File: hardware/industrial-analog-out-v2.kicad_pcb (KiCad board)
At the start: 2 copper layers, 40 x 40 mm, 54 parts, among them P1 CON-SENSOR2, P2 CONN_8, P3 DEBUG, P4 BOOT, U1 LMR62014X, U2 XMC1XXX24, U3 DACX760, U4 DRILL, U5 DRILL, U6 DRILL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

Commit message: fix fiducials
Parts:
- D5, D6: value LED -> blue
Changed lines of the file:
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@@
-(kicad_pcb (version 4) (host pcbnew 4.0.7-e2-6376~58~ubuntu17.04.1)
+(kicad_pcb (version 4) (host pcbnew 4.0.7-e2-6376~61~ubuntu18.04.1)
   (general
     (links 115)
@@
     (mod_text_size 1.5 1.5)
     (mod_text_width 0.15)
-    (pad_size 0.45 1.75)
+    (pad_size 1.00076 1.00076)
     (pad_drill 0)
     (pad_to_mask_clearance 0)
@@
     )
     (fp_circle (center 0 0) (end 1.15062 0) (layer Dwgs.User) (width 0.01016))
-    (pad 1 smd circle (at 0 0) (size 1.00076 1.00076) (layers F.Cu F.Mask)
+    (pad 1 smd circle (at 0 0) (size 1.00076 1.00076) (layers F.Cu F.Paste F.Mask)
       (clearance 0.65024))
   )
@@
     )
     (fp_circle (center 0 0) (end 1.15062 0) (layer Dwgs.User) (width 0.01016))
-    (pad 1 smd circle (at 0 0) (size 1.00076 1.00076) (layers F.Cu F.Mask)
+    (pad 1 smd circle (at 0 0) (size 1.00076 1.00076) (layers F.Cu F.Paste F.Mask)
       (clearance 0.65024))
   )
@@
     )
     (fp_circle (center 0 0) (end 1.15062 0) (layer Dwgs.User) (width 0.01016))
-    (pad 1 smd circle (at 0 0) (size 1.00076 1.00076) (layers F.Cu F.Mask)
+    (pad 1 smd circle (at 0 0) (size 1.00076 1.00076) (layers F.Cu F.Paste F.Mask)
       (clearance 0.65024))
   )
@@
       (effects (font (size 0.2 0.2) (thickness 0.05)))
     )
-    (fp_text value LED (at 0.75 0.45 270) (layer F.Fab)
+    (fp_text value blue (at 0.75 0.45 270) (layer F.Fab)
       (effects (font (size 0.2 0.2) (thickness 0.05)))
     )
@@
       (effects (font (size 0.2 0.2) (thickness 0.05)))
     )
-    (fp_text value LED (at 0.75 0.45 270) (layer F.Fab)
+    (fp_text value blue (at 0.75 0.45 270) (layer F.Fab)
       (effects (font (size 0.2 0.2) (thickness 0.05)))
     )

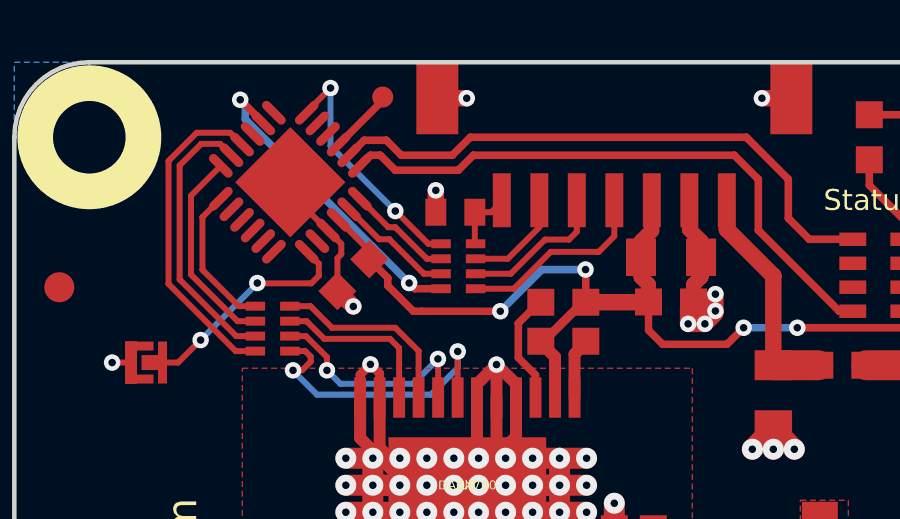
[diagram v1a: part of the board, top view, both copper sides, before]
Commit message: Change capacitor footprint(s) to C0402F
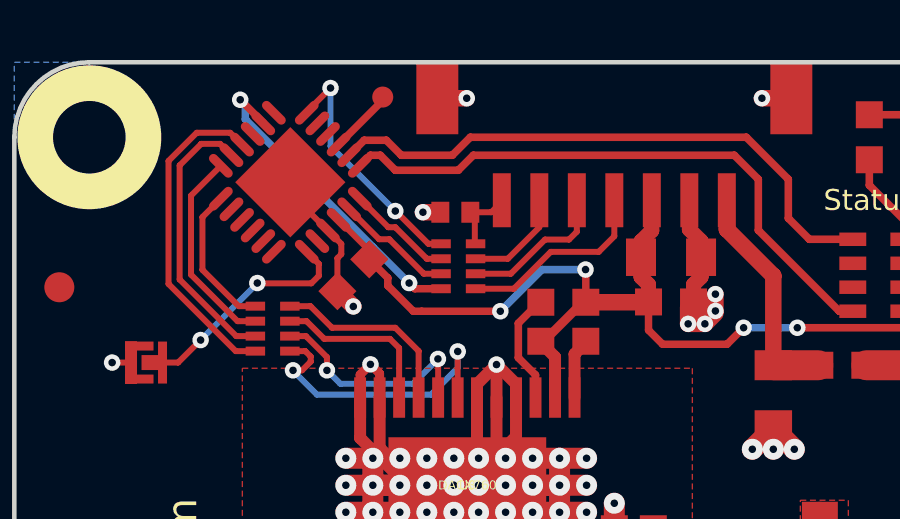
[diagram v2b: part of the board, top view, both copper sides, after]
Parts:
- C12: footprint kicad-libraries:C0402E -> kicad-libraries:C0402F
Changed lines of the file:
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@@
-(kicad_pcb (version 4) (host pcbnew 4.0.7-e2-6376~61~ubuntu18.04.1)
+(kicad_pcb (version 4) (host pcbnew 4.0.2+dfsg1-stable)
   (general
     (links 115)
     (no_connects 0)
-    (area 13.58714 79.144999 156.455001 195.49)
+    (area 13.43714 79.144999 156.455001 194.74)
     (thickness 1.6)
     (drawings 22)
@@
     )
   )
-  (module kicad-libraries:C0402E (layer F.Cu)
-    (at 130.3 85 180)
-    (attr smd)
-    (fp_text reference C12 (at 0 0.125 180) (layer F.Fab)
-      (effects (font (size 0.2 0.2) (thickness 0.05)))
-    )
-    (fp_text value 220pF (at 0 -0.275 180) (layer F.Fab)
-      (effects (font (size 0.2 0.2) (thickness 0.05)))
-    )
-    (fp_line (start -0.8509 -0.44958) (end 0.8509 -0.44958) (layer F.Fab) (width 0.001))
-    (fp_line (start 0.8509 -0.44958) (end 0.8509 0.44958) (layer F.Fab) (width 0.001))
-    (fp_line (start 0.8509 0.44958) (end -0.8509 0.44958) (layer F.Fab) (width 0.001))
-    (fp_line (start -0.8509 0.44958) (end -0.8509 -0.44958) (layer F.Fab) (width 0.001))
-    (pad 1 smd rect (at -0.65 0 180) (size 0.7 0.9) (layers F.Cu F.Paste F.Mask)
-      (net 26 "Net-(C12-Pad1)"))
-    (pad 2 smd rect (at 0.65 0 180) (size 0.7 0.9) (layers F.Cu F.Paste F.Mask)
-      (net 2 GND))
-    (model Capacitors_SMD/C_0402.wrl
-      (at (xyz 0 0 0))
-      (scale (xyz 1 1 1))
-      (rotate (xyz 0 0 0))
-    )
-  )
   (module kicad-libraries:C0805 (layer F.Cu)
     (at 137.49 86.5)
@@
     )
   )
+  (module kicad-libraries:C0402F (layer F.Cu)
+    (at 130.3 85 180)
+    (fp_text reference C12 (at 0.1 0.15 180) (layer F.Fab)
+      (effects (font (size 0.2 0.2) (thickness 0.05)))
+    )
+    (fp_text value 220pF (at 0 -0.15 180) (layer F.Fab)
+      (effects (font (size 0.2 0.2) (thickness 0.05)))
+    )
+    (fp_line (start -0.9 -0.45) (end 0.9 -0.45) (layer F.Fab) (width 0.025))
+    (fp_line (start 0.9 -0.45) (end 0.9 0.45) (layer F.Fab) (width 0.025))
+    (fp_line (start 0.9 0.45) (end -0.9 0.45) (layer F.Fab) (width 0.025))
+    (fp_line (start -0.9 0.45) (end -0.9 -0.45) (layer F.Fab) (width 0.025))
+    (pad 2 smd rect (at 0.5 0 180) (size 0.6 0.7) (layers F.Cu F.Paste F.Mask)
+      (net 2 GND))
+    (pad 1 smd rect (at -0.5 0 180) (size 0.6 0.7) (layers F.Cu F.Paste F.Mask)
+      (net 26 "Net-(C12-Pad1)"))
+    (model Capacitors_SMD/C_0402.wrl
+      (at (xyz 0 0 0))
+      (scale (xyz 1 1 1))
+      (rotate (xyz 0 0 0))
+    )
+  )
   (gr_text Out (at 147.3 84.6) (layer F.SilkS)
     (effects (font (size 0.7 0.7) (thickness 0.15)))
@@
   (segment (start 133.62354 91.17646) (end 133.62354 89.82364) (width 0.4) (layer F.Cu) (net 1))
   (segment (start 134.7001 88) (end 134.65 88) (width 0.4) (layer F.Cu) (net 1))
+  (segment (start 129.8 85) (end 129.22 85) (width 0.55) (layer F.Cu) (net 2))
+  (via (at 129.22 85) (size 0.55) (drill 0.25) (layers F.Cu B.Cu) (net 2))
   (segment (start 128.3 100.25) (end 127.7 100.25) (width 0.55) (layer F.Cu) (net 2))
   (segment (start 127.7 100.25) (end 127.65 100.3) (width 0.55) (layer F.Cu) (net 2))
@@
   (segment (start 126.39033 87.63033) (end 126.9 88.14) (width 0.55) (layer F.Cu) (net 2))
   (via (at 126.9 88.14) (size 0.55) (drill 0.25) (layers F.Cu B.Cu) (net 2))
-  (segment (start 129.65 85) (end 129.65 84.27) (width 0.55) (layer F.Cu) (net 2))
-  (via (at 129.65 84.27) (size 0.55) (drill 0.25) (layers F.Cu B.Cu) (net 2))
   (via (at 127.65 100.3) (size 0.55) (drill 0.25) (layers F.Cu B.Cu) (net 2))
   (segment (start 126.425 106.9) (end 126.425 101.525) (width 0.254) (layer B.Cu) (net 2))

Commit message: specify processor
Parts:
- U2: value XMC1XXX24 -> XMC11XX24
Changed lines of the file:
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@@
-(kicad_pcb (version 4) (host pcbnew 4.0.2+dfsg1-stable)
+(kicad_pcb (version 4) (host pcbnew 4.0.7-e2-6376~61~ubuntu18.04.1)
   (general
     (links 115)
     (no_connects 0)
-    (area 13.43714 79.144999 156.455001 194.74)
+    (area 13.58714 79.144999 156.455001 195.49)
     (thickness 1.6)
     (drawings 22)
@@
       (effects (font (size 0.3 0.3) (thickness 0.075)))
     )
-    (fp_text value XMC1XXX24 (at 0 0.8 45) (layer F.Fab)
+    (fp_text value XMC11XX24 (at 0 0.8 45) (layer F.Fab)
       (effects (font (size 0.3 0.3) (thickness 0.075)))
     )

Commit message: specify processor
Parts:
- U2: value XMC11XX24 -> XMC1100

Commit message: fix inductor footprints
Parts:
- L1, L3, L4: footprint kicad-libraries:C0603F -> kicad-libraries:R0603F

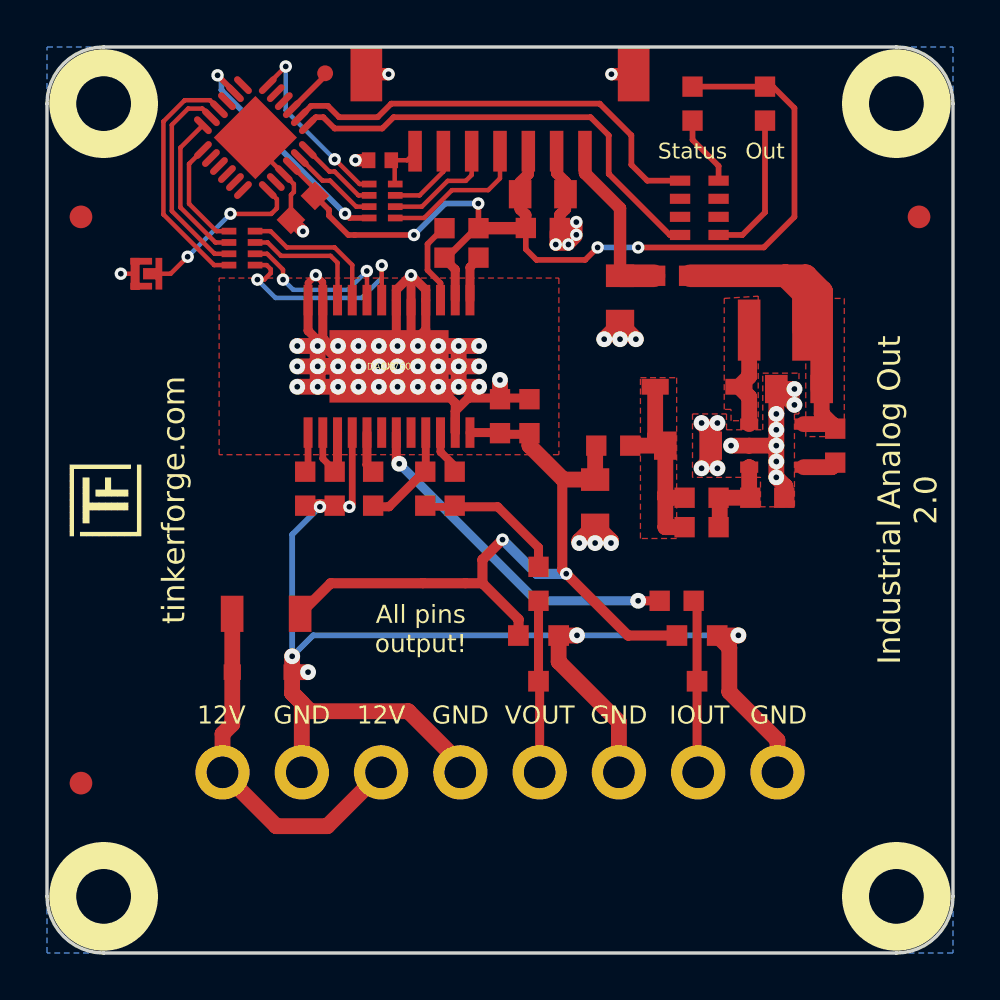
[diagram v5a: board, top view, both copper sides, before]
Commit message: New standart layout. Switched to Kicad 6
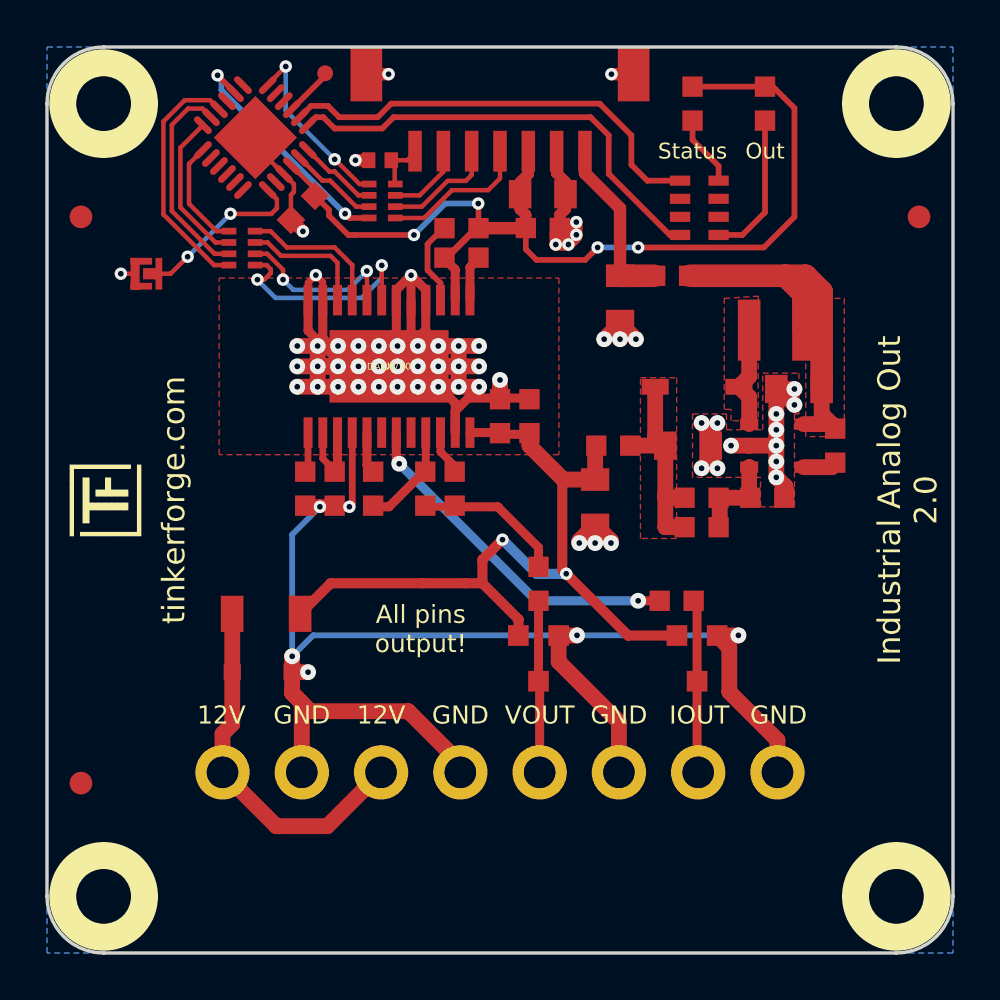
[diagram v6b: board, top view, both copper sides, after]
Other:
- net class Default removed

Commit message: Data Cleanup
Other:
- board text added: "Copyright Tinkerforge GmbH 2023. This documentation describes Open Hardware and is licensed under the CERN OHL v. 1.1. You may redistribute and modify this documentation under the terms of the CERN OHL v.1.1. (http://ohwr.org/cernohl). This documentation is distributed WITHOUT ANY EXPRESS OR IMPLIED WARRANTY, INCLUDING OF MERCHANTABILITY, SATISFACTORY QUALITY AND FITNESS FOR A PARTICULAR PURPOSE.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"
- board text removed: "Copyright Tinkerforge GmbH 2018. This documentation describes Open Hardware and is licensed under the CERN OHL v. 1.1. You may redistribute and modify this documentation under the terms of the CERN OHL v.1.1. (http://ohwr.org/cernohl). This documentation is distributed WITHOUT ANY EXPRESS OR IMPLIED WARRANTY, INCLUDING OF MERCHANTABILITY, SATISFACTORY QUALITY AND FITNESS FOR A PARTICULAR PURPOSE.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"
